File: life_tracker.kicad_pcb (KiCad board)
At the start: 2 copper layers, 2 parts, among them J1 TACTILE-NAV-SWITCH

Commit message: Initial pass at schematic.
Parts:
- removed LED1: 7-SEGMENT-4DIGIT-GREEN-CC, LED:7-SEGMENT-4DIGIT-YOUNGSUN
- added C1: 0.1uF, Capacitor_SMD:C_0805_2012Metric_Pad1.18x1.45mm_HandSolder, F.Cu at (128.0, 57.0)
- added R1: 4.7k, Resistor_SMD:R_1206_3216Metric_Pad1.30x1.75mm_HandSolder, F.Cu at (129.6, 108.0)
- added R2: 4.7k, Resistor_SMD:R_1206_3216Metric_Pad1.30x1.75mm_HandSolder, F.Cu at (104.5, 61.0)
- added R3: 4.7k, Resistor_SMD:R_1206_3216Metric_Pad1.30x1.75mm_HandSolder, F.Cu at (104.5, 64.0)
- added R4: 39k, Resistor_SMD:R_1206_3216Metric_Pad1.30x1.75mm_HandSolder, F.Cu at (145.0, 70.0)
- added R5: 39k, Resistor_SMD:R_1206_3216Metric_Pad1.30x1.75mm_HandSolder, F.Cu at (103.0, 74.0)
- added U1: WeMos_D1_mini, Module:WEMOS_D1_mini_light, F.Cu at (140.0, 126.0)
- added U10: 5611AH, Display_7Segment:7SegmentLED_LTS6760_LTS6780, F.Cu at (112.0, 97.0)
- added U11: 5611AH, Display_7Segment:7SegmentLED_LTS6760_LTS6780, F.Cu at (125.5, 97.0)
- added U12: 5611AH, Display_7Segment:7SegmentLED_LTS6760_LTS6780, F.Cu at (139.0, 97.0)
- added U13: LSHD-7803, Display_7Segment:HDSP-A151, F.Cu at (103.0, 87.0)
- added U2: PTS526-tactile-button, MyFootprints:pts526-tactile-button, F.Cu at (147.0, 124.0)
- added U3: PTS526-tactile-button, MyFootprints:pts526-tactile-button, F.Cu at (147.0, 116.2)
- added U4: MAX6959BAEE+, MyFootprints:MAX6959BAEE&plus_, F.Cu at (127.0, 64.0)
- added U5: BAW56, MyFootprints:SOT95P240X110-3N, F.Cu at (107.0, 106.0)
- added U6: BAW56, MyFootprints:SOT95P240X110-3N, F.Cu at (103.0, 111.0)
- added U7: BAW56, MyFootprints:SOT95P240X110-3N, F.Cu at (112.0, 109.0)
- added U8: BAW56, MyFootprints:SOT95P240X110-3N, F.Cu at (148.0, 109.0)
- added U9: I2C_128x64_OLED, MyFootprints:I2C_128x64_OLED, F.Cu at (127.0, 64.5)
- moved J1 6.32 mm to (107.8, 119.7)
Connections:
- J1 pad 6: Net-(J1-Pad6) -> Net-(J1-Pad1)

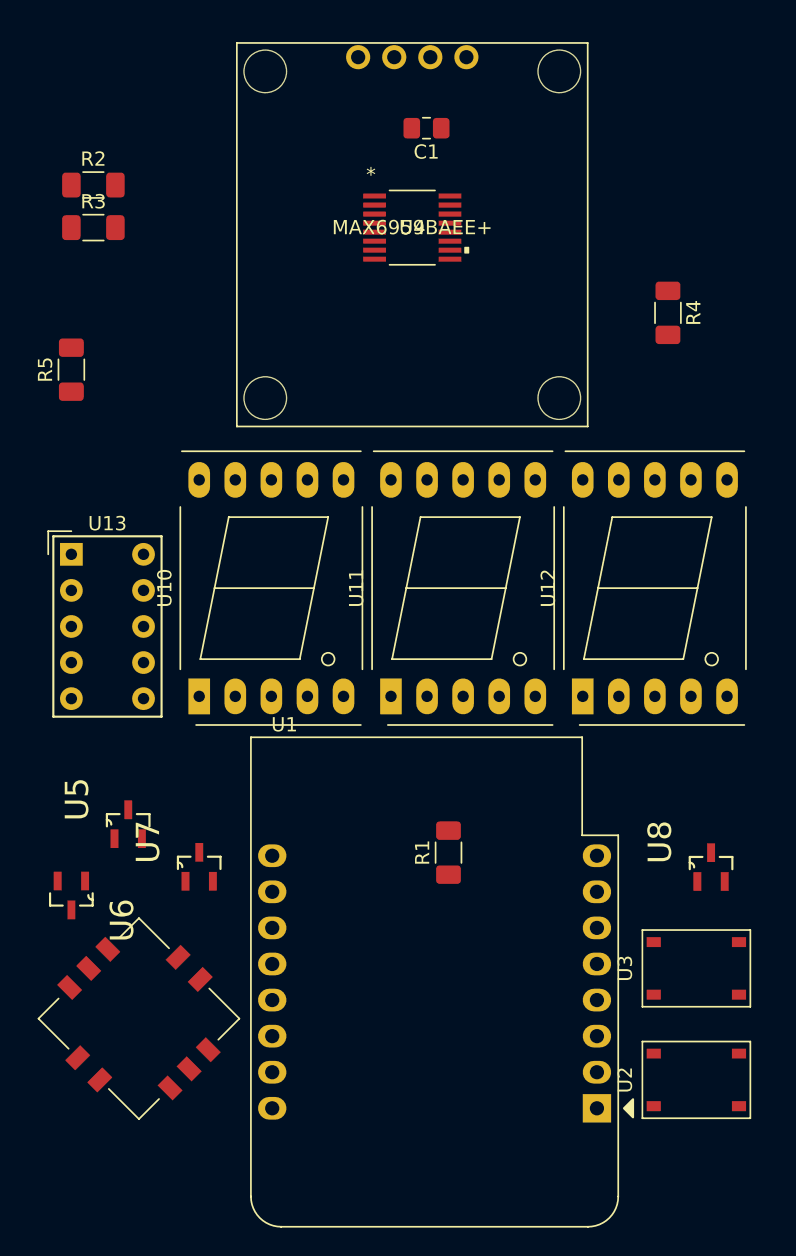
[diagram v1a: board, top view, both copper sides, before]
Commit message: started routing PCB, need to flip D1
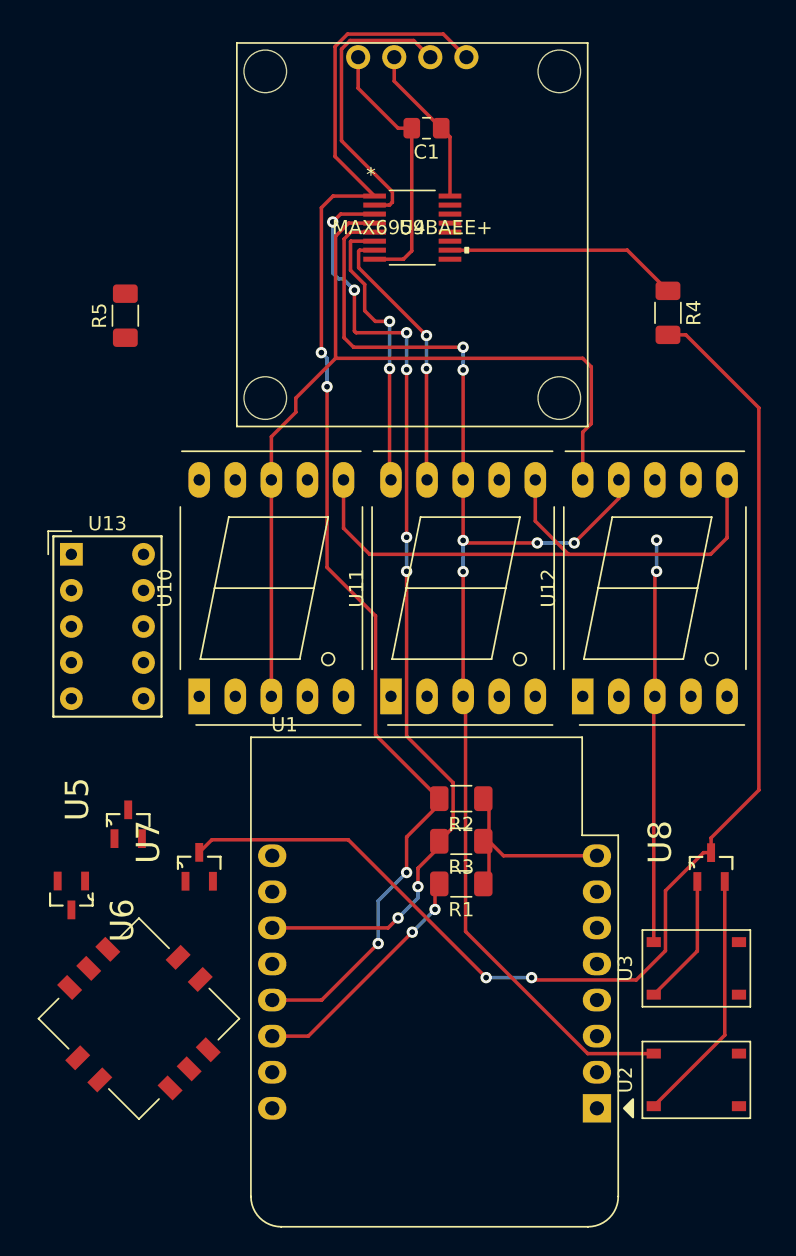
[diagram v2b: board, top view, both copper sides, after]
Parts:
- moved R2 50.4 mm to (130.4, 104.2), turned to 180 degrees
- moved R3 50.4 mm to (130.4, 107.2), turned to 180 degrees
- moved R5 5.37 mm to (106.8, 70.2)
- moved R1 2.38 mm to (130.4, 110.2), turned to 180 degrees
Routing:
- net Net-(R2-Pad2): track 0.00 -> 92.7 mm, vias 0 -> 4
- net Net-(J1-Pad7): track 0.00 -> 89.8 mm, vias 0 -> 6
- net Net-(R4-Pad2): track 0.00 -> 87.9 mm, vias 0 -> 2
- net Net-(R3-Pad2): track 0.00 -> 68.9 mm, vias 0 -> 8
- net Net-(J1-Pad1): track 0.00 -> 63.9 mm
- net Net-(J1-Pad9): track 0.00 -> 53.1 mm, vias 0 -> 4
- net Net-(U10-Pad6): track 0.00 -> 43.0 mm
- net Net-(R1-Pad2): track 0.00 -> 37.8 mm, vias 0 -> 2
- net Net-(J1-Pad2): track 0.00 -> 19.2 mm, vias 0 -> 2
- net GND: track 0.00 -> 18.6 mm
- net Net-(U2-Pad3): track 0.00 -> 17.9 mm
- net Net-(R4-Pad1): track 0.00 -> 16.5 mm
- net Net-(R1-Pad1): track 0.00 -> 14.0 mm
- net +5V: track 0.00 -> 11.4 mm
- net Net-(U3-Pad3): track 0.00 -> 9.24 mm
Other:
- copper layers 2 -> 4

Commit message: Finished second revision.
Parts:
- removed R5: 39k, Resistor_SMD:R_1206_3216Metric_Pad1.30x1.75mm_HandSolder
- removed U10, U11, U12: 5611AH, Display_7Segment:7SegmentLED_LTS6760_LTS6780
- removed U13: LSHD-7803, Display_7Segment:HDSP-A151
- removed the U2 at (147.0, 124.0)
- removed U6, U7, U8: BAW56, MyFootprints:SOT95P240X110-3N
- added C1: 10uF, Capacitor_SMD:C_0805_2012Metric_Pad1.18x1.45mm_HandSolder, F.Cu at (106.2, 62.8)
- added LED1: 7-SEGMENT-4DIGIT-10MM-KGREEN-CC, MyFootprints:7-SEGMENT-4DIGIT-YOUNGSUN, F.Cu at (127.0, 86.0)
- added RV1: 100k, MyFootprints:TC33-SMD-Trimpot, F.Cu at (111.2, 63.5)
- R4: value 39k -> 4.7k
- U3: value PTS526-tactile-button -> AS1115-BSST; footprint MyFootprints:pts526-tactile-button -> Package_SO:QSOP-24_3.9x8.7mm_P0.635mm
- U4: value MAX6959BAEE+ -> PTS526-tactile-button; footprint MyFootprints:MAX6959BAEE&plus_ -> MyFootprints:pts526-tactile-button
- U5: value BAW56 -> PTS526-tactile-button; footprint MyFootprints:SOT95P240X110-3N -> MyFootprints:pts526-tactile-button
- moved U3 60.3 mm to (106.0, 72.0)
- moved U4 42.9 mm to (147.0, 102.0)
- moved U5 41.8 mm to (147.0, 118.0), turned to 0 degrees
- moved R4 37.5 mm to (109.7, 57.2), turned to 0 degrees
- moved U1 33.2 mm to (117.0, 102.0), turned to 0 degrees
- moved C2 23.2 mm to (106.2, 65.0)
- moved R3 13.0 mm to (123.5, 118.2), turned to 0 degrees
- moved R2 12.3 mm to (123.7, 114.4), turned to 0 degrees
- moved J1 7.69 mm to (107.5, 112.0)
- moved R1 6.80 mm to (123.7, 110.4), turned to 0 degrees
- moved U2 0.50 mm to (127.0, 65.0)
- renumbered C1 to C2, U9 to U2
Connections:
- J1 pad 3: Net-(J1-Pad3) -> Net-(J1-Pad10)
- J1 pad 4: Net-(J1-Pad4) -> Net-(J1-Pad10)
- J1 pad 5: Net-(J1-Pad5) -> Net-(J1-Pad10)
- J1 pad 6: Net-(J1-Pad1) -> Net-(J1-Pad6)
- J1 pad 8: Net-(J1-Pad8) -> Net-(J1-Pad10)
- R4 pad 1: Net-(R4-Pad1) -> +5V
- U3 pad 1: Net-(J1-Pad9) -> Net-(R1-Pad2)
- U4 pad 1: Net-(R2-Pad2) -> Net-(LED1-Pad16)
- U4 pad 2: Net-(R1-Pad2) -> Net-(U4-Pad2)
- U4 pad 3: Net-(R3-Pad2) -> Net-(J1-Pad10)
- U4 pad 4: Net-(J1-Pad1) -> Net-(U4-Pad4)
- U5 pad 1: Net-(J1-Pad3) -> Net-(LED1-Pad14)
- U5 pad 2: Net-(J1-Pad4) -> Net-(U5-Pad2)
- U5 pad 3: Net-(R5-Pad1) -> Net-(J1-Pad10)
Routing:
- net Net-(J1-Pad10): track 0.00 -> 122.6 mm, vias 0 -> 2
- net +5V: track 11.4 -> 115.4 mm, vias 0 -> 3
- net GND: track 18.6 -> 110.6 mm, vias 0 -> 2
- net Net-(R1-Pad2): track 37.8 -> 124.1 mm, vias 2 -> 1
- net Net-(R4-Pad2): track 87.9 -> 4.87 mm, vias 2 -> 0
- net Net-(LED1-Pad16): track 0.00 -> 70.9 mm, vias 0 -> 3
- net Net-(LED1-Pad14): track 0.00 -> 64.8 mm, vias 0 -> 1
- net Net-(J1-Pad2): track 19.2 -> 76.8 mm
- net Net-(J1-Pad6): track 0.00 -> 55.4 mm, vias 0 -> 2
- net Net-(LED1-Pad8): track 0.00 -> 52.1 mm, vias 0 -> 2
- net Net-(LED1-Pad6): track 0.00 -> 48.7 mm, vias 0 -> 2
- net Net-(R2-Pad2): track 92.7 -> 135.9 mm
- net Net-(U10-Pad6): track 43.0 -> 0.00 mm
- net Net-(LED1-Pad1): track 0.00 -> 40.6 mm
- net Net-(LED1-Pad7): track 0.00 -> 40.5 mm, vias 0 -> 2
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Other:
- copper layers 4 -> 2

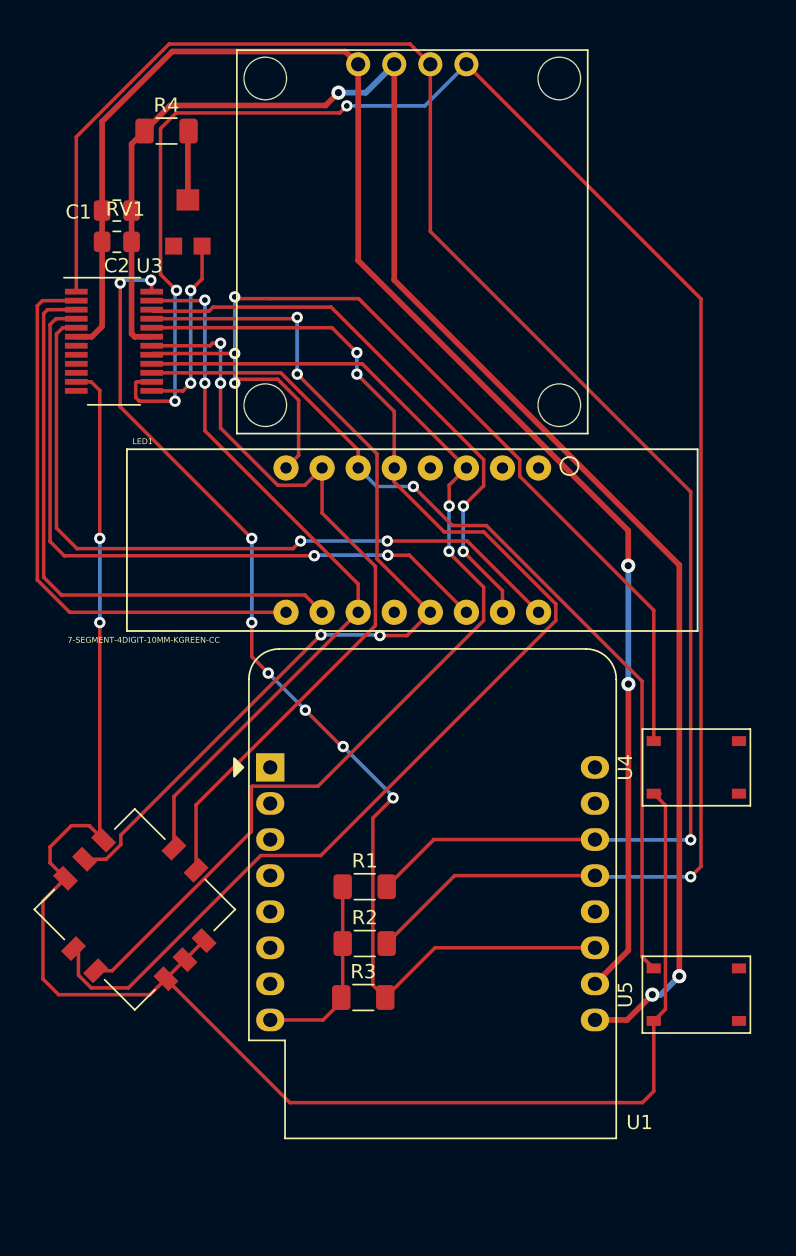
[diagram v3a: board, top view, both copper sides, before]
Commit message: Moved resisters out from under d1.
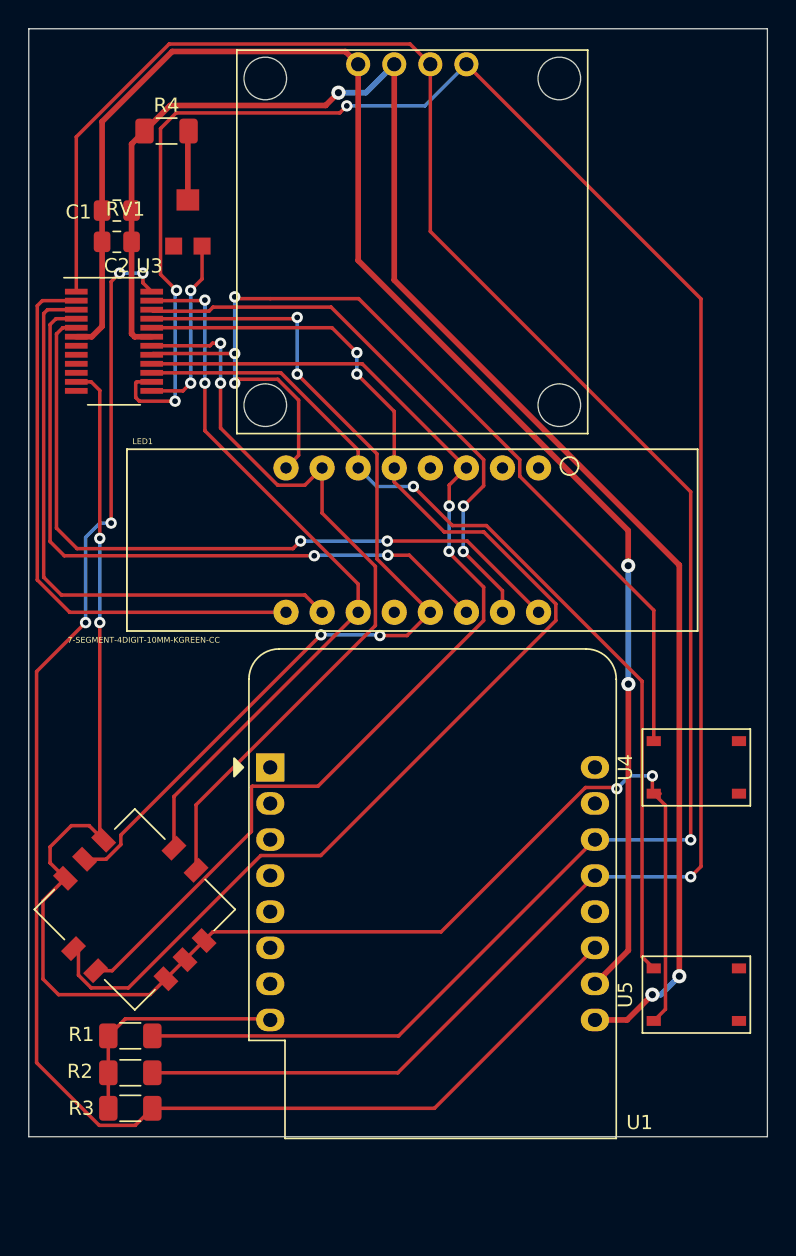
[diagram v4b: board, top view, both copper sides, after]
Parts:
- moved R1 19.6 mm to (107.2, 120.9)
- moved R2 18.8 mm to (107.2, 123.5)
- moved R3 18.2 mm to (107.2, 126.0)
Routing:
- net Net-(R3-Pad2): track 78.6 -> 108.0 mm, vias 8 -> 4
- net Net-(R1-Pad2): track 124.1 -> 144.9 mm
- net Net-(R2-Pad2): track 135.9 -> 156.2 mm
- net Net-(J1-Pad10): track 122.6 -> 117.1 mm, vias 2 -> 4
- net Net-(R1-Pad1): track 13.7 -> 17.0 mm
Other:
- board outline added: 52 x 78 mm

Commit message: Add art.
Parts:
- added svg2mod: G***, MyFootprints:plains_walker, F.Cu at (140.5, 51.3)

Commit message: Added squirrel.
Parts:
- added svg2mod: G***, MyFootprints:squirrel2, B.Cu at (138.4, 103.2)
